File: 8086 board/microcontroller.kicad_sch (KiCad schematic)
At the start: 21 parts, among them J2 USB, U20 ATmega328P, U21 74HC595, U22 74HC595, U23 74HC595, U24 74HC165, U25 74HC165, U26 CH340C, Y1 16MHz

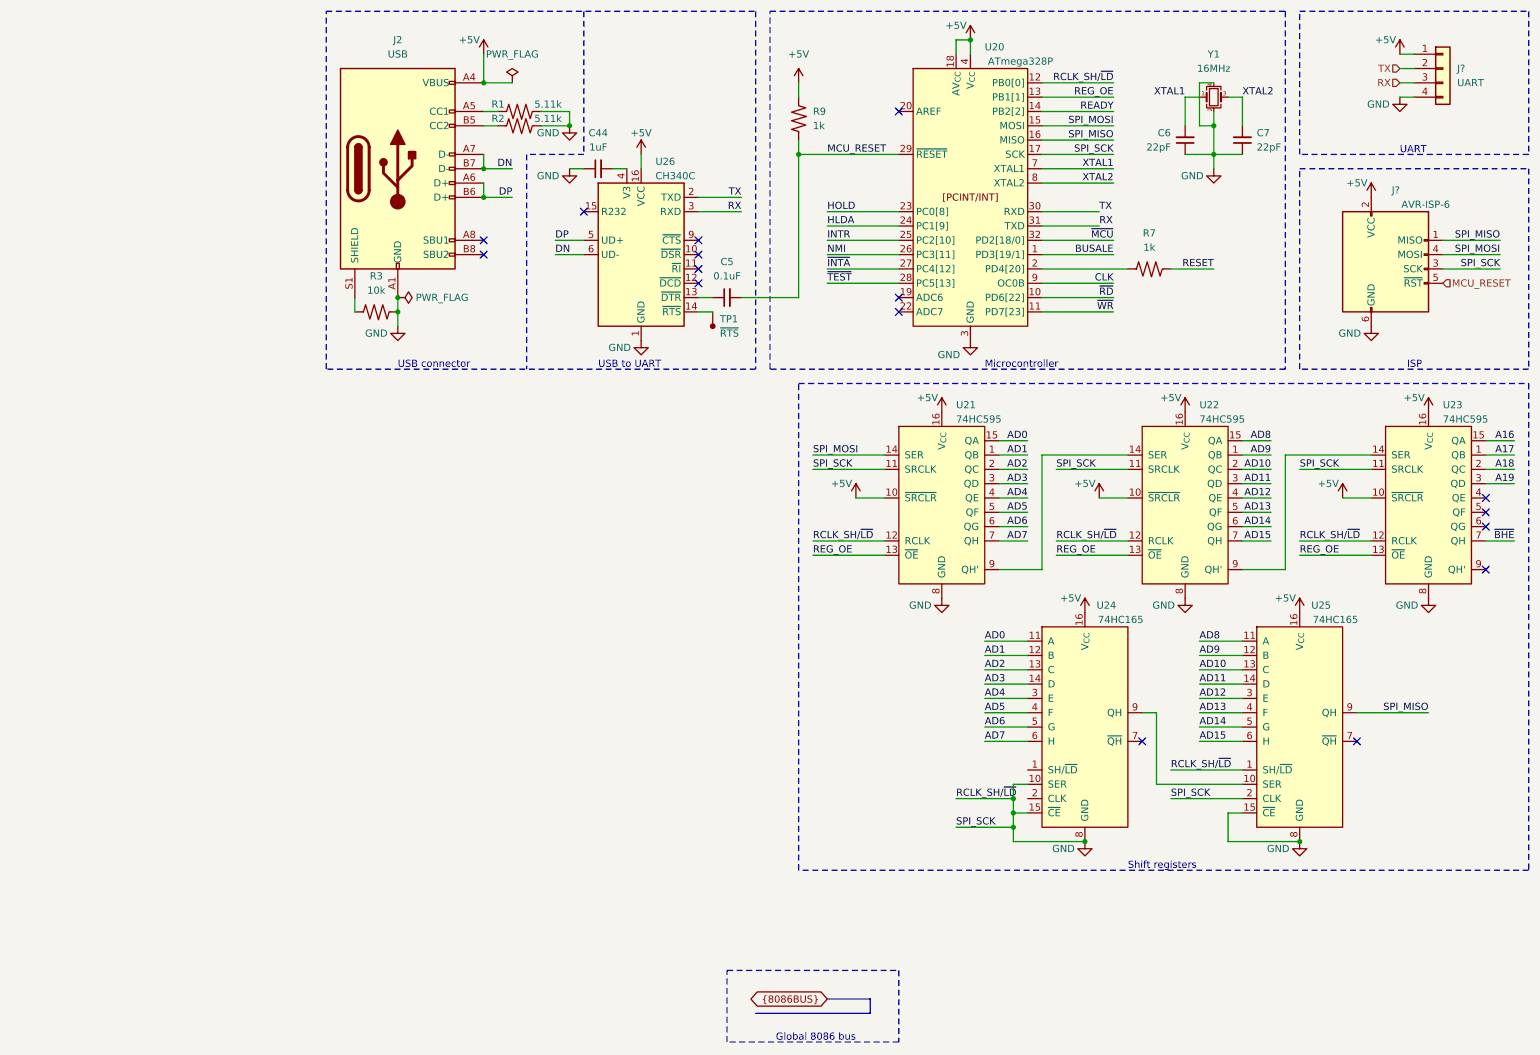
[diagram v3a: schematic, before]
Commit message: PCB: different layout
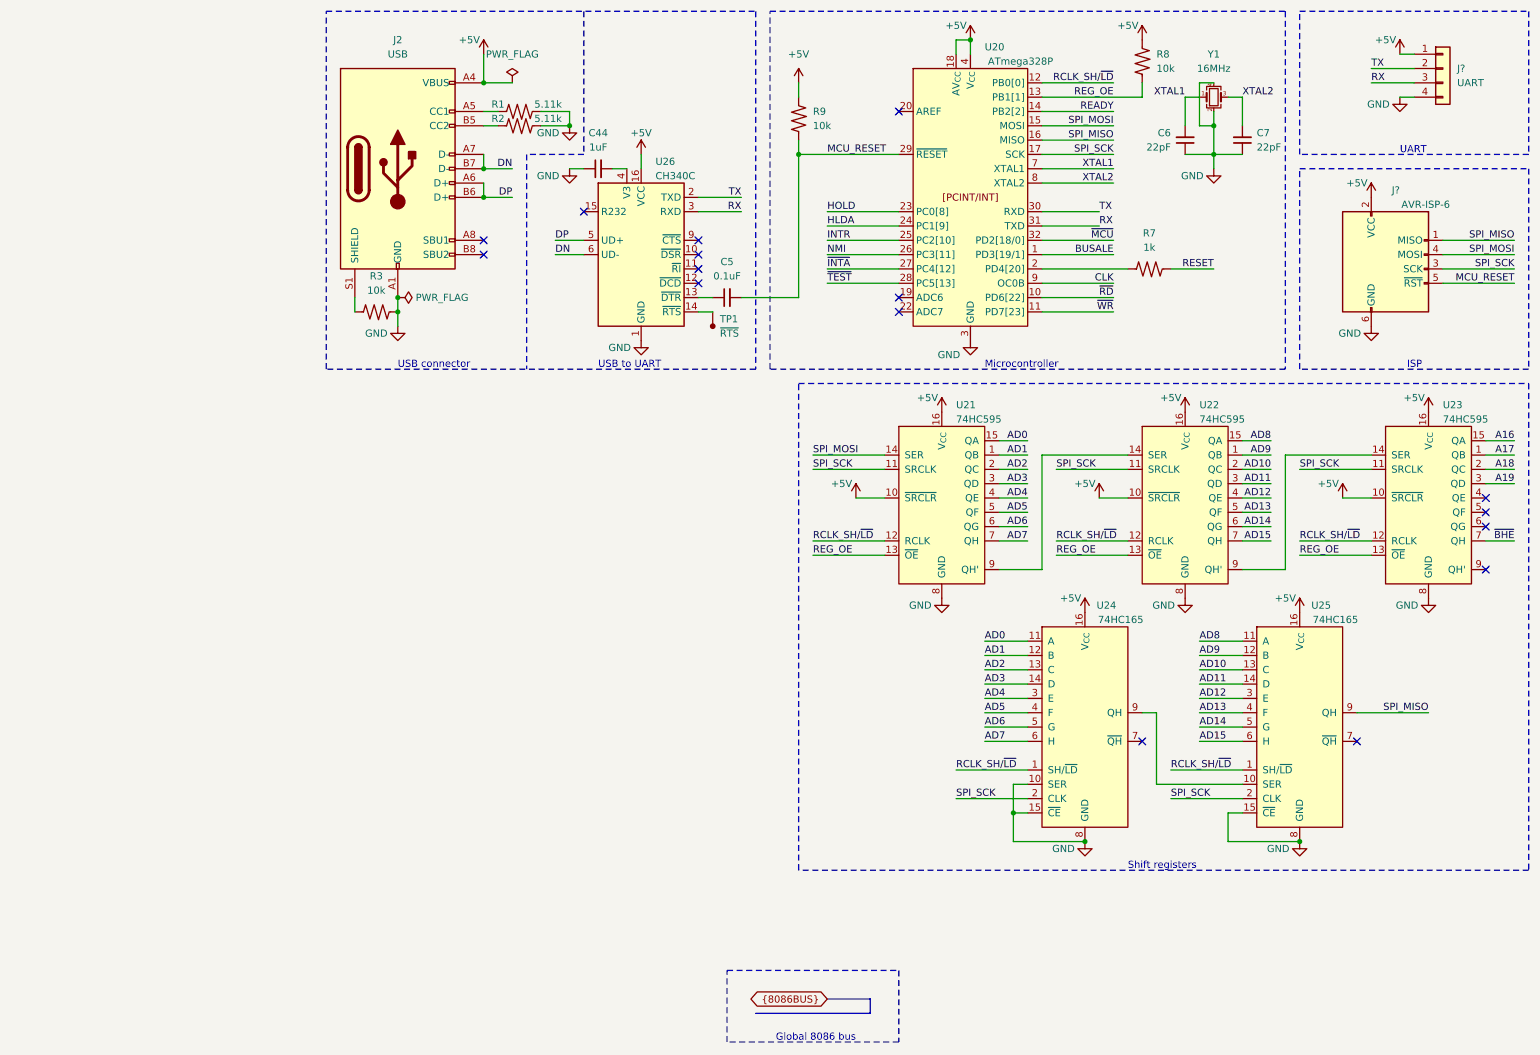
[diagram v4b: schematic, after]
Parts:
- added R8: 10k, Resistor_SMD:R_0603_1608Metric_Pad0.98x0.95mm_HandSolder, symbol 8086PC:R
- R9: value 1k -> 10k
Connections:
- net +5V: now also R8.2
- net GND: no longer J?.3 (SCK), U20.12 (PB0[0]), U20.17 (PB5[5]), U21.11 (SRCLK), U21.12 (RCLK), U22.11 (SRCLK), U22.12 (RCLK), U23.11 (SRCLK), U23.12 (RCLK), U25.1 (SH/~{LD}), U25.2 (CLK)
- net REG_OE: now also R8.1
- net RCLK_SH/~{LD}: now reaches U24.1 (SH/~{LD})
- net RCLK_SH/~{LD}: now also U20.12 (PB0[0]), U21.12 (RCLK), U22.12 (RCLK), U23.12 (RCLK), U25.1 (SH/~{LD})
- net SPI_SCK: now reaches U24.2 (CLK)
- net SPI_SCK: now also J?.3 (SCK), U20.17 (PB5[5]), U21.11 (SRCLK), U22.11 (SRCLK), U23.11 (SRCLK), U25.2 (CLK)
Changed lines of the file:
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@@
     (comment 1 "Open Source: github.com/EldadHellerman/8086-computer")
   )
+  (junction (at 193.04 154.94) (diameter 0) (color 0 0 0 0)
+  )
   (junction (at 228.6 33.02) (diameter 0) (color 0 0 0 0)
   )
@@
   (junction (at 99.06 25.4) (diameter 0) (color 0 0 0 0)
   )
-  (junction (at 193.04 157.48) (diameter 0) (color 0 0 0 0)
-  )
   (junction (at 154.94 38.1) (diameter 0) (color 0 0 0 0)
   )
@@
   (junction (at 185.42 17.78) (diameter 0) (color 0 0 0 0)
   )
-  (junction (at 193.04 152.4) (diameter 0) (color 0 0 0 0)
-  )
   (junction (at 99.06 40.64) (diameter 0) (color 0 0 0 0)
   )
@@
   )
   (junction (at 205.74 160.02) (diameter 0) (color 0 0 0 0)
-  )
-  (junction (at 193.04 154.94) (diameter 0) (color 0 0 0 0)
   )
   (junction (at 99.06 45.72) (diameter 0) (color 0 0 0 0)
@@
     (stroke (width 0) (type default))
   )
-  (wire (pts (xy 269.24 55.88) (xy 279.4 55.88))
+  (wire (pts (xy 269.24 55.88) (xy 281.94 55.88))
     (stroke (width 0) (type default))
   )
@@
     (stroke (width 0) (type default))
   )
-  (wire (pts (xy 182.88 152.4) (xy 193.04 152.4))
-    (stroke (width 0) (type default))
-  )
   (wire (pts (xy 231.14 160.02) (xy 243.84 160.02))
     (stroke (width 0) (type default))
@@
     (stroke (width 0) (type default))
   )
+  (wire (pts (xy 182.88 147.32) (xy 195.58 147.32))
+    (stroke (width 0) (type default))
+  )
   (wire (pts (xy 198.12 43.18) (xy 210.82 43.18))
     (stroke (width 0) (type default))
@@
     (stroke (width 0) (type default))
   )
-  (wire (pts (xy 269.24 58.42) (xy 279.4 58.42))
+  (wire (pts (xy 269.24 58.42) (xy 281.94 58.42))
     (stroke (width 0) (type default))
   )
@@
   )
   (bus (pts (xy 160.02 187.96) (xy 167.64 187.96))
-    (stroke (width 0) (type default))
-  )
-  (wire (pts (xy 193.04 149.86) (xy 193.04 152.4))
     (stroke (width 0) (type default))
   )
@@
     (stroke (width 0) (type dash))
   )
+  (wire (pts (xy 281.94 60.96) (xy 269.24 60.96))
+    (stroke (width 0) (type default))
+  )
   (wire (pts (xy 187.96 132.08) (xy 195.58 132.08))
     (stroke (width 0) (type default))
@@
     (stroke (width 0) (type default))
   )
-  (wire (pts (xy 193.04 160.02) (xy 193.04 157.48))
-    (stroke (width 0) (type default))
-  )
-  (wire (pts (xy 193.04 157.48) (xy 193.04 154.94))
+  (wire (pts (xy 193.04 154.94) (xy 193.04 160.02))
     (stroke (width 0) (type default))
   )
@@
     (stroke (width 0) (type default))
   )
-  (wire (pts (xy 261.62 25.4) (xy 264.16 25.4))
+  (wire (pts (xy 256.54 25.4) (xy 264.16 25.4))
     (stroke (width 0) (type default))
   )
@@
     (stroke (width 0) (type default))
   )
-  (wire (pts (xy 198.12 27.94) (xy 210.82 27.94))
+  (wire (pts (xy 198.12 27.94) (xy 215.9 27.94))
     (stroke (width 0) (type default))
   )
@@
     (stroke (width 0) (type default))
   )
-  (wire (pts (xy 261.62 22.86) (xy 264.16 22.86))
+  (wire (pts (xy 256.54 22.86) (xy 264.16 22.86))
     (stroke (width 0) (type default))
   )
@@
     (stroke (width 0) (type default))
   )
-  (wire (pts (xy 193.04 157.48) (xy 182.88 157.48))
-    (stroke (width 0) (type default))
-  )
   (wire (pts (xy 154.94 25.4) (xy 154.94 27.94))
     (stroke (width 0) (type default))
@@
     (stroke (width 0) (type default))
   )
-  (wire (pts (xy 269.24 53.34) (xy 279.4 53.34))
+  (wire (pts (xy 269.24 53.34) (xy 281.94 53.34))
     (stroke (width 0) (type default))
   )
@@
     (stroke (width 0) (type dash))
   )
-  (wire (pts (xy 193.04 149.86) (xy 195.58 149.86))
+  (wire (pts (xy 182.88 152.4) (xy 195.58 152.4))
     (stroke (width 0) (type default))
   )
@@
     (stroke (width 0) (type default))
   )
-  (wire (pts (xy 193.04 152.4) (xy 193.04 154.94))
-    (stroke (width 0) (type default))
-  )
   (wire (pts (xy 223.52 33.02) (xy 223.52 27.94))
     (stroke (width 0) (type default))
@@
     (stroke (width 0) (type default))
   )
+  (wire (pts (xy 195.58 149.86) (xy 193.04 149.86))
+    (stroke (width 0) (type default))
+  )
   (wire (pts (xy 154.94 38.1) (xy 172.72 38.1))
     (stroke (width 0) (type default))
@@
     (stroke (width 0) (type default))
   )
+  (wire (pts (xy 193.04 149.86) (xy 193.04 154.94))
+    (stroke (width 0) (type default))
+  )
   (wire (pts (xy 233.68 149.86) (xy 218.44 149.86))
+    (stroke (width 0) (type default))
+  )
+  (wire (pts (xy 215.9 25.4) (xy 215.9 27.94))
     (stroke (width 0) (type default))
   )
@@
     (effects (font (size 1.27 1.27)) (justify left bottom))
   )
+  (label "TX" (at 256.54 22.86 0) (fields_autoplaced)
+    (effects (font (size 1.27 1.27)) (justify left bottom))
+  )
   (label "AD5" (at 187.96 137.16 0) (fields_autoplaced)
     (effects (font (size 1.27 1.27)) (justify left bottom))
@@
     (effects (font (size 1.27 1.27)) (justify left bottom))
   )
-  (label "SPI_MOSI" (at 279.4 55.88 180) (fields_autoplaced)
+  (label "SPI_MOSI" (at 281.94 55.88 180) (fields_autoplaced)
     (effects (font (size 1.27 1.27)) (justify right bottom))
   )
@@
     (effects (font (size 1.27 1.27)) (justify left bottom))
   )
-  (label "SPI_MISO" (at 279.4 53.34 180) (fields_autoplaced)
+  (label "SPI_MISO" (at 281.94 53.34 180) (fields_autoplaced)
     (effects (font (size 1.27 1.27)) (justify right bottom))
   )
@@
     (effects (font (size 1.27 1.27)) (justify right bottom))
   )
-  (label "RCLK_SH{slash}~{LD}" (at 182.88 152.4 0) (fields_autoplaced)
+  (label "RCLK_SH{slash}~{LD}" (at 182.88 147.32 0) (fields_autoplaced)
     (effects (font (size 1.27 1.27)) (justify left bottom))
   )
@@
     (effects (font (size 1.27 1.27)) (justify right bottom))
   )
-  (label "SPI_SCK" (at 182.88 157.48 0) (fields_autoplaced)
-    (effects (font (size 1.27 1.27)) (justify left bottom))
-  )
-  (label "SPI_SCK" (at 279.4 58.42 180) (fields_autoplaced)
+  (label "SPI_SCK" (at 182.88 152.4 0) (fields_autoplaced)
+    (effects (font (size 1.27 1.27)) (justify left bottom))
+  )
+  (label "SPI_SCK" (at 281.94 58.42 180) (fields_autoplaced)
     (effects (font (size 1.27 1.27)) (justify right bottom))
   )
@@
   )
   (label "AD6" (at 187.96 139.7 0) (fields_autoplaced)
+    (effects (font (size 1.27 1.27)) (justify left bottom))
+  )
+  (label "MCU_RESET" (at 281.94 60.96 180) (fields_autoplaced)
+    (effects (font (size 1.27 1.27)) (justify right bottom))
+  )
+  (label "RX" (at 256.54 25.4 0) (fields_autoplaced)
     (effects (font (size 1.27 1.27)) (justify left bottom))
   )
@@
     )
   )
-  (hierarchical_label "RX" (shape input) (at 261.62 25.4 180) (fields_autoplaced)
-    (effects (font (size 1.27 1.27)) (justify right))
-  )
-  (hierarchical_label "MCU_RESET" (shape input) (at 269.24 60.96 0) (fields_autoplaced)
-    (effects (font (size 1.27 1.27)) (justify left))
-  )
-  (hierarchical_label "TX" (shape input) (at 261.62 22.86 180) (fields_autoplaced)
-    (effects (font (size 1.27 1.27)) (justify right))
+  (symbol (lib_id "8086PC:R") (at 215.9 22.86 90) (unit 1)
+    (in_bom yes) (on_board yes) (dnp no) (fields_autoplaced)
+    (property "Reference" "R8" (at 218.44 20.32 90)
+      (effects (font (size 1.27 1.27)) (justify right))
+    )
+    (property "Value" "10k" (at 218.44 22.86 90)
+      (effects (font (size 1.27 1.27)) (justify right))
+    )
+    (property "Footprint" "Resistor_SMD:R_0603_1608Metric_Pad0.98x0.95mm_HandSolder" (at 215.9 21.336 0)
+      (effects (font (size 1.27 1.27)) hide)
+    )
+    (property "Datasheet" "" (at 215.9 21.336 0)
+      (effects (font (size 1.27 1.27)) hide)
+    )
+    (pin "1")
+    (pin "2")
+    (instances
+      (project "8086 board"
+        (path "/3749a875-289f-4484-aa3f-51b8984af853/424ba84c-5097-43d2-b6a3-f93a63e78a77"
+          (reference "R8") (unit 1)
+        )
+      )
+    )
   )
   (symbol (lib_id "power:+5V") (at 223.52 83.82 0) (unit 1)
@@
         (path "/3749a875-289f-4484-aa3f-51b8984af853"
           (reference "#PWR0101") (unit 1)
+        )
+      )
+    )
+  )
+  (symbol (lib_id "power:+5V") (at 215.9 17.78 0) (mirror y) (unit 1)
+    (in_bom yes) (on_board yes) (dnp no)
+    (property "Reference" "#PWR028" (at 215.9 21.59 0)
+      (effects (font (size 1.27 1.27)) hide)
+    )
+    (property "Value" "+5V" (at 213.36 15.24 0)
+      (effects (font (size 1.27 1.27)))
+    )
+    (property "Footprint" "" (at 215.9 17.78 0)
+      (effects (font (size 1.27 1.27)) hide)
+    )
+    (property "Datasheet" "" (at 215.9 17.78 0)
+      (effects (font (size 1.27 1.27)) hide)
+    )
+    (pin "1")
+    (instances
+      (project "8086 board"
+        (path "/3749a875-289f-4484-aa3f-51b8984af853/424ba84c-5097-43d2-b6a3-f93a63e78a77"
+          (reference "#PWR028") (unit 1)
         )
       )
@@
       (effects (font (size 1.27 1.27)) (justify right))
     )
-    (property "Value" "1k" (at 157.48 33.02 90)
+    (property "Value" "10k" (at 157.48 33.02 90)
       (effects (font (size 1.27 1.27)) (justify right))
     )

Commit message: PCB: layout and routing of IO, shift registers, and MCU
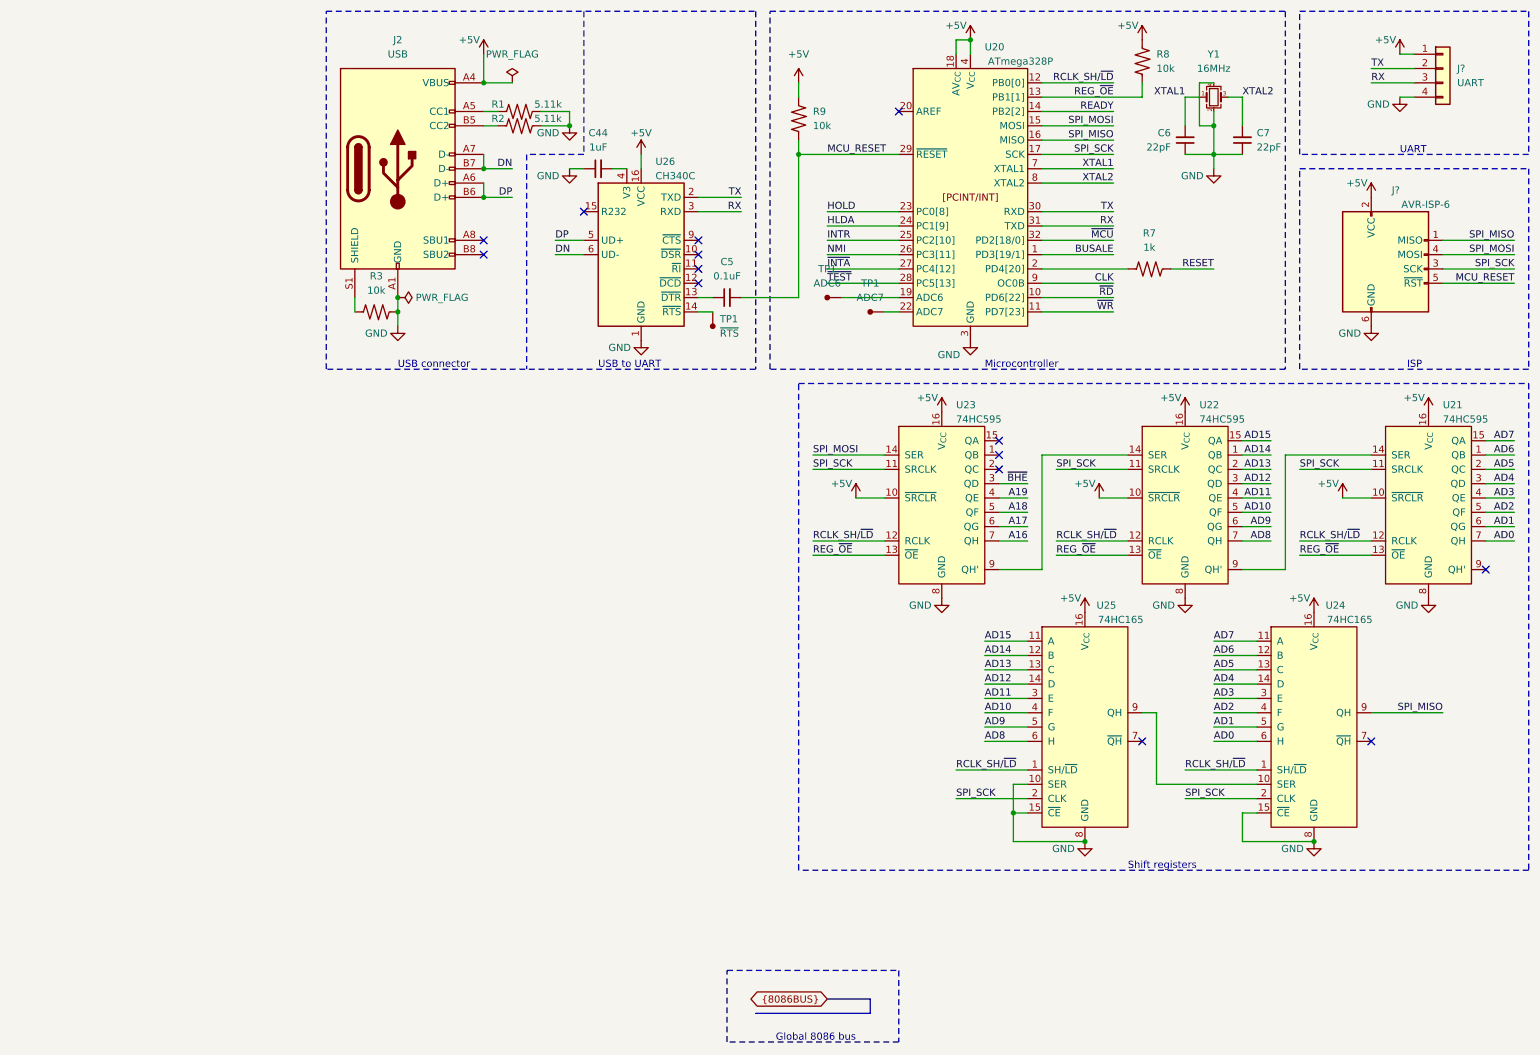
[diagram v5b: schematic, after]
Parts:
- added TP1: ADC6, TestPoint:TestPoint_Pad_1.5x1.5mm, symbol 8086PC:TestPoint
- added TP1: ADC7, TestPoint:TestPoint_Pad_1.5x1.5mm, symbol 8086PC:TestPoint
- TP1: footprint TestPoint:TestPoint_Pad_1.5x1.5mm -> TestPoint:TestPoint_Pad_1.0x1.0mm
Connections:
- net A16: now also U23.7 (QH); no longer U23.15 (QA)
- net A17: now also U23.6 (QG); no longer U23.1 (QB)
- net A18: now also U23.5 (QF); no longer U23.2 (QC)
- net A19: now also U23.4 (QE); no longer U23.3 (QD)
- net AD0: now also U21.7 (QH), U24.6 (H); no longer U21.15 (QA), U24.11 (A)
- net AD1: now also U21.6 (QG), U24.5 (G); no longer U21.1 (QB), U24.12 (B)
- net AD10: now also U22.5 (QF), U25.4 (F); no longer U22.2 (QC), U25.13 (C)
- net AD11: now also U22.4 (QE), U25.3 (E); no longer U22.3 (QD), U25.14 (D)
- net AD12: now also U22.3 (QD), U25.14 (D); no longer U22.4 (QE), U25.3 (E)
- net AD13: now also U22.2 (QC), U25.13 (C); no longer U22.5 (QF), U25.4 (F)
- net AD14: now also U22.1 (QB), U25.12 (B); no longer U22.6 (QG), U25.5 (G)
- net AD15: now also U22.15 (QA), U25.11 (A); no longer U22.7 (QH), U25.6 (H)
- net AD2: now also U21.5 (QF), U24.4 (F); no longer U21.2 (QC), U24.13 (C)
- net AD3: now also U21.4 (QE), U24.3 (E); no longer U21.3 (QD), U24.14 (D)
- net AD4: now also U21.3 (QD), U24.14 (D); no longer U21.4 (QE), U24.3 (E)
- net AD5: now also U21.2 (QC), U24.13 (C); no longer U21.5 (QF), U24.4 (F)
- net AD6: now also U21.1 (QB), U24.12 (B); no longer U21.6 (QG), U24.5 (G)
- net AD7: now also U21.15 (QA), U24.11 (A); no longer U21.7 (QH), U24.6 (H)
- net AD8: now also U22.7 (QH), U25.6 (H); no longer U22.15 (QA), U25.11 (A)
- net AD9: now also U22.6 (QG), U25.5 (G); no longer U22.1 (QB), U25.12 (B)
- net GND: now also U25.10 (SER); no longer U24.10 (SER)
- net SPI_MISO: now also U24.9 (QH); no longer U25.9 (QH)
- net SPI_MOSI: now also U23.14 (SER); no longer U21.14 (SER)
- net ~{BHE}: now also U23.3 (QD); no longer U23.7 (QH)
- net at U21.9 (QH'): no longer U22.14 (SER)
- net at U20.19 (ADC6): now also TP1.1
- net at U20.22 (ADC7): now also TP1.1
- net at U22.9 (QH'): now also U21.14 (SER); no longer U23.14 (SER)
- net at U23.9 (QH'): now also U22.14 (SER)
- net REG_OE renamed REG_~{OE}
- new net: U24.10 (SER), U25.9 (QH)
- no-connect marks 16 -> 14
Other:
- moved on the sheet: U21, U23, U24, U25
